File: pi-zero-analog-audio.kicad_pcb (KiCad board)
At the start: 2 copper layers, 65 x 30 mm, 22 parts, among them J1 GPIO, J2 SJ1-3555NG-BE, U1 LP5907MFX-3.3, U2 74LVC2G34

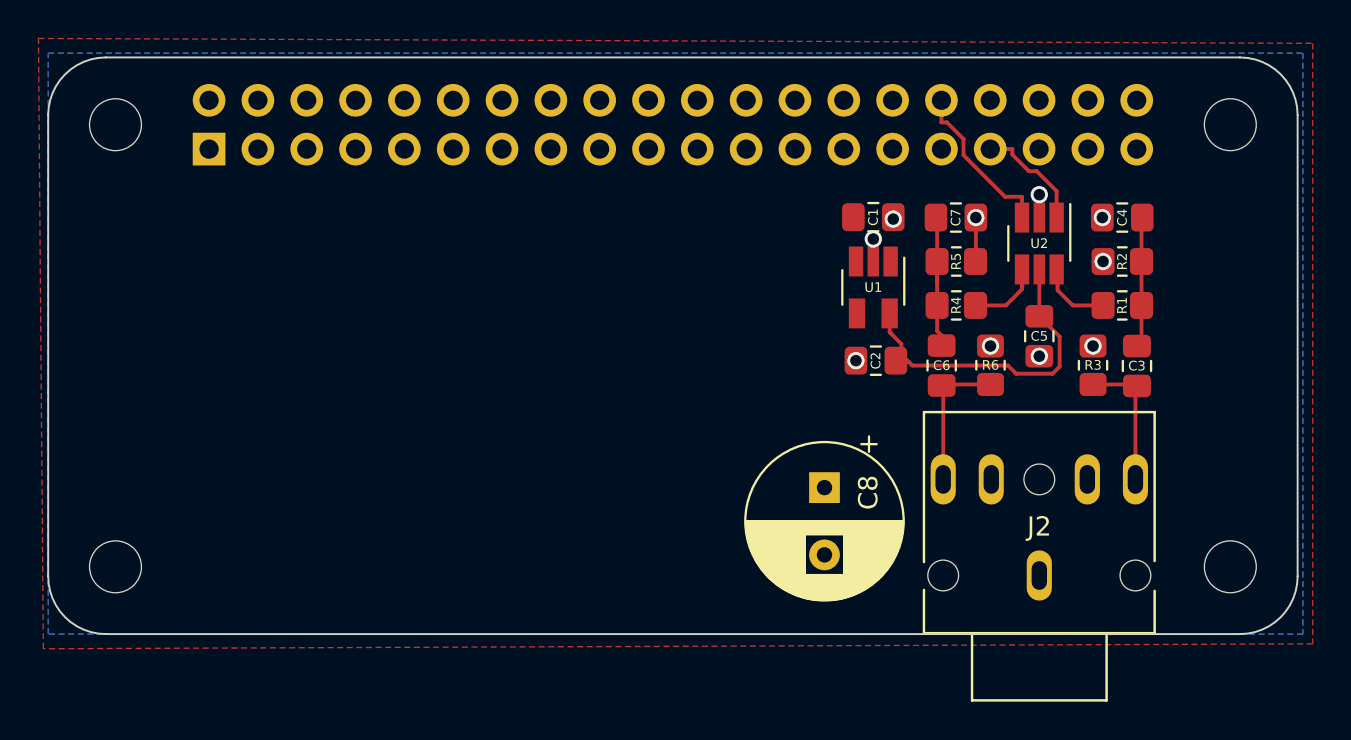
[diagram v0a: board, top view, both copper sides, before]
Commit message: Adding PAM8403D based amplifier
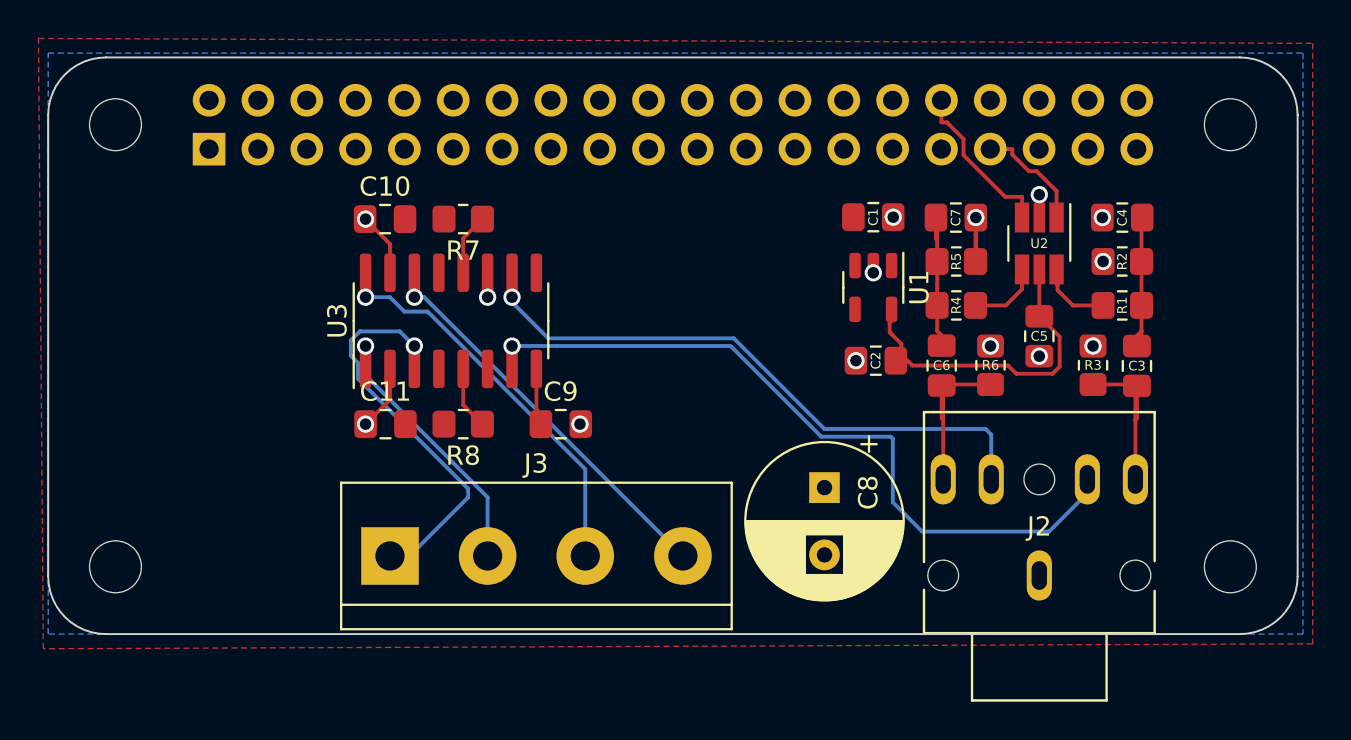
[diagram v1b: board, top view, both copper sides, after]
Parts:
- added C10: 1u, Capacitor_SMD:C_0805_2012Metric_Pad1.18x1.45mm_HandSolder, F.Cu at (117.5, 78.4)
- added C11: 1u, Capacitor_SMD:C_0805_2012Metric_Pad1.18x1.45mm_HandSolder, F.Cu at (117.5, 89.1)
- added C9: 100n, Capacitor_SMD:C_0805_2012Metric_Pad1.18x1.45mm_HandSolder, F.Cu at (126.7, 89.1)
- added J3: Screw_Terminal_01x04, TerminalBlock:TerminalBlock_bornier-4_P5.08mm, F.Cu at (117.8, 95.9)
- added R7: 10k, Resistor_SMD:R_0805_2012Metric_Pad1.20x1.40mm_HandSolder, F.Cu at (121.6, 78.4)
- added R8: 10K, Resistor_SMD:R_0805_2012Metric_Pad1.20x1.40mm_HandSolder, F.Cu at (121.6, 89.1)
- added U3: PAM8403D, Package_SO:SOP-16_3.9x9.9mm_P1.27mm, F.Cu at (121.0, 83.7)
- U1: footprint Package_TO_SOT_SMD:SOT-23-5_HandSoldering -> Package_TO_SOT_SMD:SOT-23-5
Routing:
- net /AMP_L: track 0.00 -> 37.8 mm, vias 0 -> 1
- net /AMP_R: track 0.00 -> 31.6 mm, vias 0 -> 1
- net /R+: track 0.00 -> 19.7 mm, vias 0 -> 1
- net /R-: track 0.00 -> 19.5 mm, vias 0 -> 1
- net /L-: track 0.00 -> 18.8 mm, vias 0 -> 1
- net /L+: track 0.00 -> 13.6 mm, vias 0 -> 1
- net GND: track 2.87 -> 11.0 mm, vias 10 -> 14
- net /MUTE: track 0.00 -> 3.29 mm
- net /SHDN: track 0.00 -> 3.21 mm
- net Net-(C9-Pad1): track 0.00 -> 2.64 mm
- net /AUDIO_R: track 7.26 -> 9.08 mm
- net /AUDIO_L: track 6.99 -> 8.79 mm
- net Net-(C3-Pad1): track 5.85 -> 6.72 mm
- net Net-(R1-Pad2): track 3.24 -> 4.07 mm
- net VCC: track 16.8 -> 17.6 mm

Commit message: Some more clearance of zone fixes
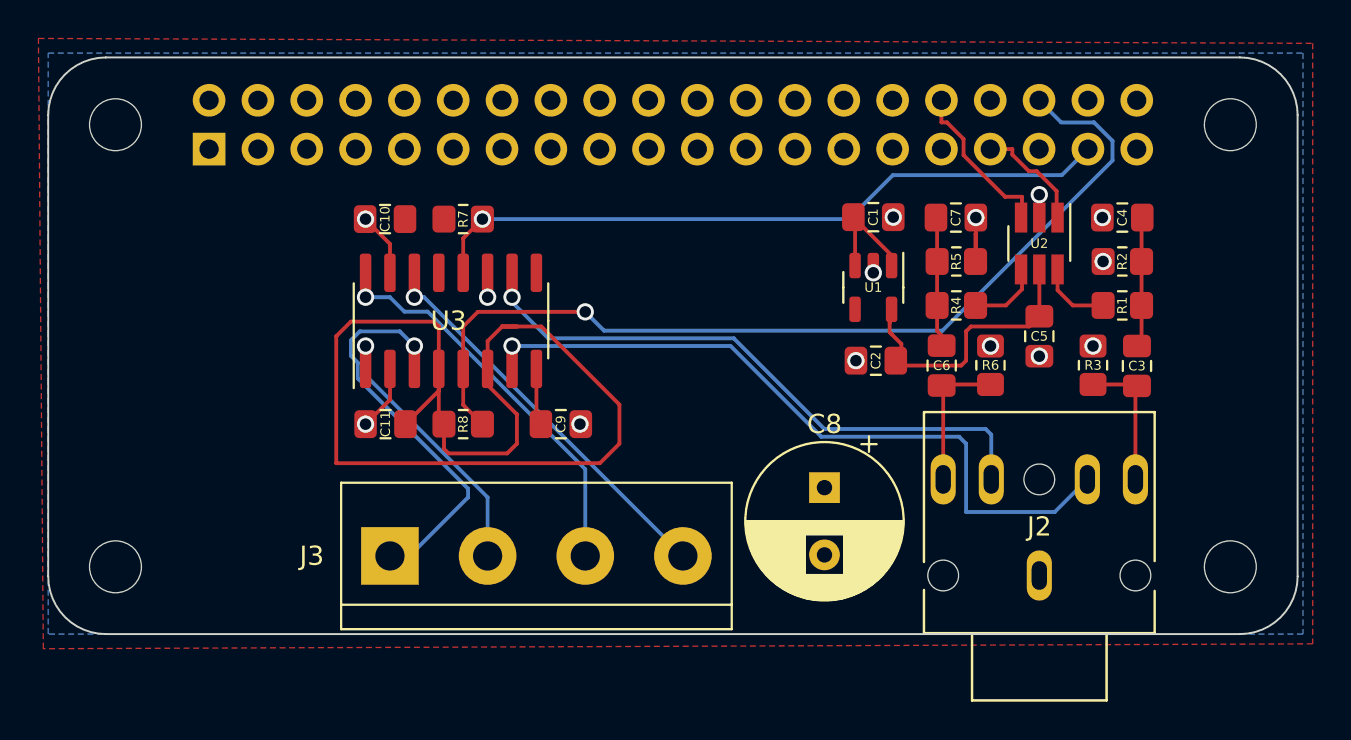
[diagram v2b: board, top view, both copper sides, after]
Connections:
- J1 pad 36: unconnected-(J1-Pad36) -> /MUTE
- J1 pad 37: unconnected-(J1-Pad37) -> /SHDN
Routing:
- net +5V: track 0.00 -> 62.6 mm
- net /MUTE: track 3.29 -> 49.4 mm, vias 0 -> 1
- net /SHDN: track 3.21 -> 36.2 mm, vias 0 -> 1
- net VCC: track 17.6 -> 14.1 mm
- net /AUDIO_R: track 9.08 -> 7.26 mm
- net /AUDIO_L: track 8.79 -> 6.99 mm
- net Net-(C6-Pad1): track 7.90 -> 6.70 mm
- net GND: track 11.0 -> 9.85 mm
- net Net-(R1-Pad2): track 4.07 -> 2.97 mm
- net Net-(C3-Pad1): track 6.72 -> 5.85 mm

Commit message: minor cleanup
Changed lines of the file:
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@@
   (segment (start 152.462 76.956) (end 152.462 78.33) (width 0.2) (layer "F.Cu") (net 25))
   (segment (start 151.023 75.9201) (end 151.426 75.9201) (width 0.2) (layer "F.Cu") (net 25))
-  (segment (start 122.86 84.76) (end 123.622 83.998) (width 0.2) (layer "F.Cu") (net 27))
-  (segment (start 123.622 83.998) (end 124.384 83.998) (width 0.254) (layer "F.Cu") (net 27))
-  (segment (start 122.86 87.046) (end 124.384 88.57) (width 0.2) (layer "F.Cu") (net 27))
+  (segment (start 122.86 84.76) (end 123.622 83.998) (width 0.254) (layer "F.Cu") (net 27))
+  (segment (start 123.622 83.998) (end 124.384 83.998) (width 0.508) (layer "F.Cu") (net 27))
   (segment (start 129.718 90.094) (end 128.702 91.11) (width 0.2) (layer "F.Cu") (net 27))
-  (segment (start 124.384 88.57) (end 124.384 90.094) (width 0.2) (layer "F.Cu") (net 27))
   (segment (start 114.986 91.11) (end 114.986 84.506) (width 0.2) (layer "F.Cu") (net 27))
   (segment (start 114.986 84.506) (end 115.748 83.744) (width 0.2) (layer "F.Cu") (net 27))
   (segment (start 122.86 86.204) (end 122.86 84.76) (width 0.2) (layer "F.Cu") (net 27))
   (segment (start 123.876 90.602) (end 120.828 90.602) (width 0.2) (layer "F.Cu") (net 27))
+  (segment (start 122.86 87.046) (end 124.13 88.316) (width 0.508) (layer "F.Cu") (net 27))
   (segment (start 120.32 86.204) (end 120.32 87.343) (width 0.2) (layer "F.Cu") (net 27))
   (segment (start 120.828 90.602) (end 120.59 90.364) (width 0.2) (layer "F.Cu") (net 27))
+  (segment (start 124.384 90.094) (end 124.13 89.84) (width 0.2) (layer "F.Cu") (net 27))
   (segment (start 124.384 83.998) (end 125.654 83.998) (width 0.2) (layer "F.Cu") (net 27))
-  (segment (start 120.32 86.204) (end 120.32 88.808) (width 0.2) (layer "F.Cu") (net 27))
+  (segment (start 120.32 86.204) (end 120.32 88.808) (width 0.508) (layer "F.Cu") (net 27))
   (segment (start 125.654 83.998) (end 129.718 88.062) (width 0.2) (layer "F.Cu") (net 27))
   (segment (start 128.702 91.11) (end 114.986 91.11) (width 0.2) (layer "F.Cu") (net 27))
-  (segment (start 120.32 87.343) (end 118.585 89.078) (width 0.2) (layer "F.Cu") (net 27))
+  (segment (start 120.32 87.343) (end 118.585 89.078) (width 0.508) (layer "F.Cu") (net 27))
   (segment (start 120.59 90.364) (end 120.59 89.078) (width 0.2) (layer "F.Cu") (net 27))
   (segment (start 124.384 90.094) (end 123.876 90.602) (width 0.2) (layer "F.Cu") (net 27))
@@
   (segment (start 120.32 83.998) (end 120.32 86.204) (width 0.2) (layer "F.Cu") (net 27))
   (segment (start 129.718 88.062) (end 129.718 90.094) (width 0.2) (layer "F.Cu") (net 27))
+  (segment (start 124.13 89.84) (end 124.13 88.316) (width 0.2) (layer "F.Cu") (net 27))
   (segment (start 120.066 83.744) (end 120.32 83.998) (width 0.2) (layer "F.Cu") (net 27))
   (segment (start 156.562 87.169) (end 156.562 91.952) (width 0.2) (layer "F.Cu") (net 30))
